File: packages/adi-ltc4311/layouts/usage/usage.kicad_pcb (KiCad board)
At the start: 2 copper layers, 3 parts

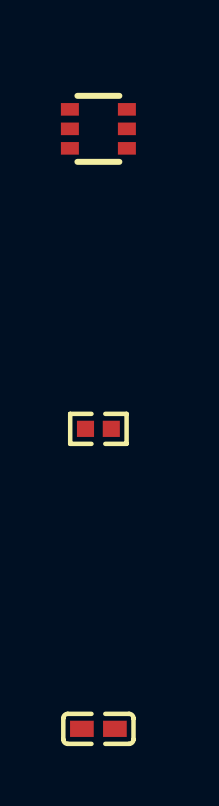
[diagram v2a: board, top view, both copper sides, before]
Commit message: Upgrade Packages: Narayans Half (#185)
* adi-ad5693r

* fix frozen

* prjc-teensy_4_1

* rp2040

* adi-adxl375: Add missing usage build target to ato.yaml

* adi-ds2482s-800: Update layout files after build

* adi-ltc4311: Update layout to fix frozen build

- Updated net names (BUS1/BUS2 → SDA/SCL, gnd → GND, hv → VCC)
- Fixed footprint properties and coordinates
- Package now passes frozen build and verification

* awinic-aw9523: Update layout to fix frozen build

- Updated net names (AD0/AD1 → address_bit_0/address_bit_1, hv → VCC, gnd → GND)
- Updated GPIO line names (-line-0 → gpios[8]-line, etc.)
- Fixed footprint properties and coordinates
- Package now passes frozen build and verification

* awinic-aw9523: Bump version to 0.1.1

- Version bump due to layout updates to fix frozen build

* adi-adbms6830: Fix package verify issues

- Add has_part_removed trait to components missing pickers (atopile_logo, SPDT, analog_DPDT)
- Add missing import for has_part_removed trait
- Add exclude_checks to usage build in ato.yaml
- Update README.md to match usage.ato content
- Bump version from 0.1.2 to 0.1.3

Package now passes ato package verify -s

* indicator-leds: Update layout and bump version

- Updated PCB layout coordinates to fix frozen build issues
- Bumped version from 0.1.5 to 0.1.6
- Package now passes ato package verify -s successfully

* Bump package versions for done packages

- adi-adxl345: 0.1.1 -> 0.1.2
- adi-adxl375: 0.1.0 -> 0.1.1
- adi-ds2482s-800: 0.1.0 -> 0.1.1
- adi-ltc4311: 0.1.0 -> 0.1.1
- adi-ltc4316: 0.1.0 -> 0.1.1
- ams-tsl2591: 0.1.0 -> 0.1.1

These packages were marked as 'Done' in package-todos.md but had version
warnings during package verification. Version bumps ensure they can be
published to the registry.

* invensense-mpu6050: Update layout files and bump version to 0.1.2

* Fix picker warnings by adding has_part_removed trait to MCU modules

- Added #pragma experiment("TRAITS") to enable traits feature
- Added import has_part_removed t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
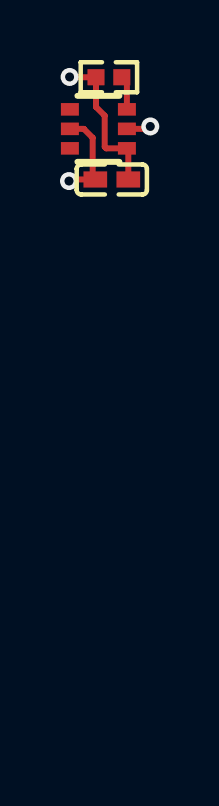
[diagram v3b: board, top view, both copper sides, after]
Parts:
- moved C1 18.3 mm to (0.45, -18.3), turned to 180 degrees
- moved R1 11.7 mm to (0.35, -21.7)
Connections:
- net -line-0 renamed SCL
- net -line-1 renamed SDA
- net gnd renamed GND
- net hv renamed VCC
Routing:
- net VCC: track 0.00 -> 5.14 mm, vias 0 -> 1
- net GND: track 0.00 -> 4.02 mm, vias 0 -> 2
- net ENABLE: track 0.00 -> 1.14 mm

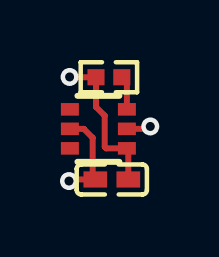
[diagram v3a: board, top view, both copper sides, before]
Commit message: adi-ltc4311: package update to v0.2.0, ato:^0.14.0
Build targets:
  default = rc0
  usage = rc0
Package Verify: rc0
Version: 0.1.1 -> 0.2.0
Requires ato: ^0.14.0
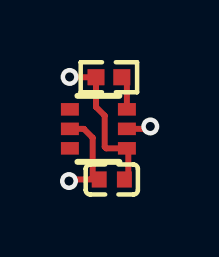
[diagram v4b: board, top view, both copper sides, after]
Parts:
- C1: value 100nF ±10% 16V X7R -> 1.0000000000000001e-07F
- R1: value 10kΩ ±1% 62.5mW -> 10000.0Ω
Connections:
- net GND renamed lv
- net VCC renamed hv

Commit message: add more git functionality to package review station
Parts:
- C1: value 1.0000000000000001e-07F -> 1.000±20.0%F
- R1: value 10000.0Ω -> 10000.0±20.0%Ω
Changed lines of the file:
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@@
 			)
 		)
-		(property "Value" "1.0000000000000001e-07F"
+		(property "Value" "1.000±20.0%F"
 			(at 0 4 180)
 			(layer "F.Fab")
@@
 			)
 		)
-		(property "Datasheet" "https://www.lcsc.com/datasheet/lcsc_datasheet_2304140030_Samsung-Electro-Mechanics-CL05B104KO5NNNC_C1525.pdf"
+		(property "Datasheet" "https://www.lcsc.com/datasheet/lcsc_datasheet_2211101700_YAGEO-CC0603KRX7R9BB104_C14663.pdf"
 			(at 0 0 180)
 			(layer "User.9")
@@
 			)
 		)
-		(property "LCSC" "C1525"
-			(at 0 0 180)
-			(layer "User.9")
-			(hide yes)
-			(effects
-				(font
-					(size 0.125 0.125)
-					(thickness 0.01875)
-				)
-			)
-		)
-		(property "Manufacturer" "Samsung Electro-Mechanics"
-			(at 0 0 180)
-			(layer "User.9")
-			(hide yes)
-			(effects
-				(font
-					(size 0.125 0.125)
-					(thickness 0.01875)
-				)
-			)
-		)
-		(property "Partnumber" "CL05B104KO5NNNC"
+		(property "LCSC" "C14663"
+			(at 0 0 180)
+			(layer "User.9")
+			(hide yes)
+			(effects
+				(font
+					(size 0.125 0.125)
+					(thickness 0.01875)
+				)
+			)
+		)
+		(property "Manufacturer" "YAGEO"
+			(at 0 0 180)
+			(layer "User.9")
+			(hide yes)
+			(effects
+				(font
+					(size 0.125 0.125)
+					(thickness 0.01875)
+				)
+			)
+		)
+		(property "Partnumber" "CC0603KRX7R9BB104"
 			(at 0 0 180)
 			(layer "User.9")
@@
 			)
 		)
-		(property "PARAM_max_voltage" "{\"type\": \"Quantity_Set_Discrete\", \"data\": {\"intervals\": {\"type\": \"Numeric_Interval_Disjoint\", \"data\": {\"intervals\": [{\"type\": \"Numeric_Interval\", \"data\": {\"min\": 16.0, \"max\": 16.0}}]}}, \"unit\": \"volt\"}}"
+		(property "PARAM_max_voltage" "{\"type\": \"Quantity_Set_Discrete\", \"data\": {\"intervals\": {\"type\": \"Numeric_Interval_Disjoint\", \"data\": {\"intervals\": [{\"type\": \"Numeric_Interval\", \"data\": {\"min\": 50.0, \"max\": 50.0}}]}}, \"unit\": \"volt\"}}"
 			(at 0 0 180)
 			(layer "User.9")
@@
 			)
 		)
-		(property "capacitance" "1.0000000000000001e-07±10.0%F"
-			(at 0 0 0)
-			(layer "User.9")
-			(hide yes)
-		)
-		(property "max_voltage" "16.0V"
+		(property "capacitance" "1.000±20.0%F"
+			(at 0 0 0)
+			(layer "User.9")
+			(hide yes)
+		)
+		(property "max_voltage" "{ℝ+}V"
 			(at 0 0 0)
 			(layer "User.9")
@@
 			(hide yes)
 		)
-		(property "lcsc_id" "C1525"
+		(property "lcsc_id" "C14663"
 			(at 0 0 0)
 			(layer "User.9")
@@
 			)
 		)
-		(property "Value" "10000.0Ω"
+		(property "Value" "10000.0±20.0%Ω"
 			(at 0 4)
 			(layer "F.Fab")
@@
 			)
 		)
-		(property "Datasheet" "https://www.lcsc.com/datasheet/lcsc_datasheet_2411221126_UNI-ROYAL-Uniroyal-Elec-0402WGF1002TCE_C25744.pdf"
+		(property "Datasheet" "https://www.lcsc.com/datasheet/lcsc_datasheet_2206010045_UNI-ROYAL-Uniroyal-Elec-0603WAF1002T5E_C25804.pdf"
 			(at 0 0 0)
 			(layer "User.9")
@@
 			)
 		)
-		(property "LCSC" "C25744"
+		(property "LCSC" "C25804"
 			(at 0 0 0)
 			(layer "User.9")
@@
 			)
 		)
-		(property "Partnumber" "0402WGF1002TCE"
-			(at 0 0 0)
-			(layer "User.9")
-			(hide yes)
-			(effects
-				(font
-					(size 0.125 0.125)
-					(thickness 0.01875)
-				)
-			)
-		)
-		(property "PARAM_max_power" "{\"type\": \"Quantity_Set_Discrete\", \"data\": {\"intervals\": {\"type\": \"Numeric_Interval_Disjoint\", \"data\": {\"intervals\": [{\"type\": \"Numeric_Interval\", \"data\": {\"min\": 0.0625, \"max\": 0.0625}}]}}, \"unit\": \"watt\"}}"
-			(at 0 0 0)
-			(layer "User.9")
-			(hide yes)
-			(effects
-				(font
-					(size 0.125 0.125)
-					(thickness 0.01875)
-				)
-			)
-		)
-		(property "PARAM_max_voltage" "{\"type\": \"Quantity_Set_Discrete\", \"data\": {\"intervals\": {\"type\": \"Numeric_Interval_Disjoint\", \"data\": {\"intervals\": [{\"type\": \"Numeric_Interval\", \"data\": {\"min\": 50.0, \"max\": 50.0}}]}}, \"unit\": \"volt\"}}"
+		(property "Partnumber" "0603WAF1002T5E"
+			(at 0 0 0)
+			(layer "User.9")
+			(hide yes)
+			(effects
+				(font
+					(size 0.125 0.125)
+					(thickness 0.01875)
+				)
+			)
+		)
+		(property "PARAM_max_power" "{\"type\": \"Quantity_Set_Discrete\", \"data\": {\"intervals\": {\"type\": \"Numeric_Interval_Disjoint\", \"data\": {\"intervals\": [{\"type\": \"Numeric_Interval\", \"data\": {\"min\": 0.1, \"max\": 0.1}}]}}, \"unit\": \"watt\"}}"
+			(at 0 0 0)
+			(layer "User.9")
+			(hide yes)
+			(effects
+				(font
+					(size 0.125 0.125)
+					(thickness 0.01875)
+				)
+			)
+		)
+		(property "PARAM_max_voltage" "{\"type\": \"Quantity_Set_Discrete\", \"data\": {\"intervals\": {\"type\": \"Numeric_Interval_Disjoint\", \"data\": {\"intervals\": [{\"type\": \"Numeric_Interval\", \"data\": {\"min\": 75.0, \"max\": 75.0}}]}}, \"unit\": \"volt\"}}"
 			(at 0 0 0)
 			(layer "User.9")
@@
 			)
 		)
-		(property "resistance" "10000.0±1.0%Ω"
-			(at 0 0 0)
-			(layer "User.9")
-			(hide yes)
-		)
-		(property "max_power" "0.0625W"
-			(at 0 0 0)
-			(layer "User.9")
-			(hide yes)
-		)
-		(property "max_voltage" "50.0V"
-			(at 0 0 0)
-			(layer "User.9")
-			(hide yes)
-		)
-		(property "lcsc_id" "C25744"
-			(at 0 0 0)
-			(layer "User.9")
+		(property "resistance" "10000.0±20.0%Ω"
+			(at 0 0 0)
+			(layer "User.9")
+			(hide yes)
+		)
+		(property "max_power" "{ℝ+}W"
+			(at 0 0 0)
+			(layer "User.9")
+			(hide yes)
+		)
+		(property "max_voltage" "{ℝ+}V"
+			(at 0 0 0)
+			(layer "User.9")
+			(hide yes)
+		)
+		(property "lcsc_id" "C25804"
+			(at 0 0 0)
+			(layer "User.9")

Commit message: update parts
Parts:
- C1: value 1.000±20.0%F -> 1±20.0%F
- R1: value 10000.0±20.0%Ω -> {8000..12000}Ω
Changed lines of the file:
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@@
 			)
 		)
-		(property "Value" "1.000±20.0%F"
+		(property "Value" "1±20.0%F"
 			(at 0 4 180)
 			(layer "F.Fab")
@@
 			)
 		)
-		(property "capacitance" "1.000±20.0%F"
+		(property "capacitance" "1±20.0%F"
 			(at 0 0 0)
 			(layer "User.9")
@@
 			)
 		)
-		(property "Value" "10000.0±20.0%Ω"
+		(property "Value" "{8000..12000}Ω"
 			(at 0 4)
 			(layer "F.Fab")
@@
 			)
 		)
-		(property "resistance" "10000.0±20.0%Ω"
-			(at 0 0 0)
-			(layer "User.9")
+		(property "resistance" "{8000..12000}Ω"
+			(at 0 0 0)
+			(layer "User.9")
